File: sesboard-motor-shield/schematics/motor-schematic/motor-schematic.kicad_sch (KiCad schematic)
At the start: 0 parts

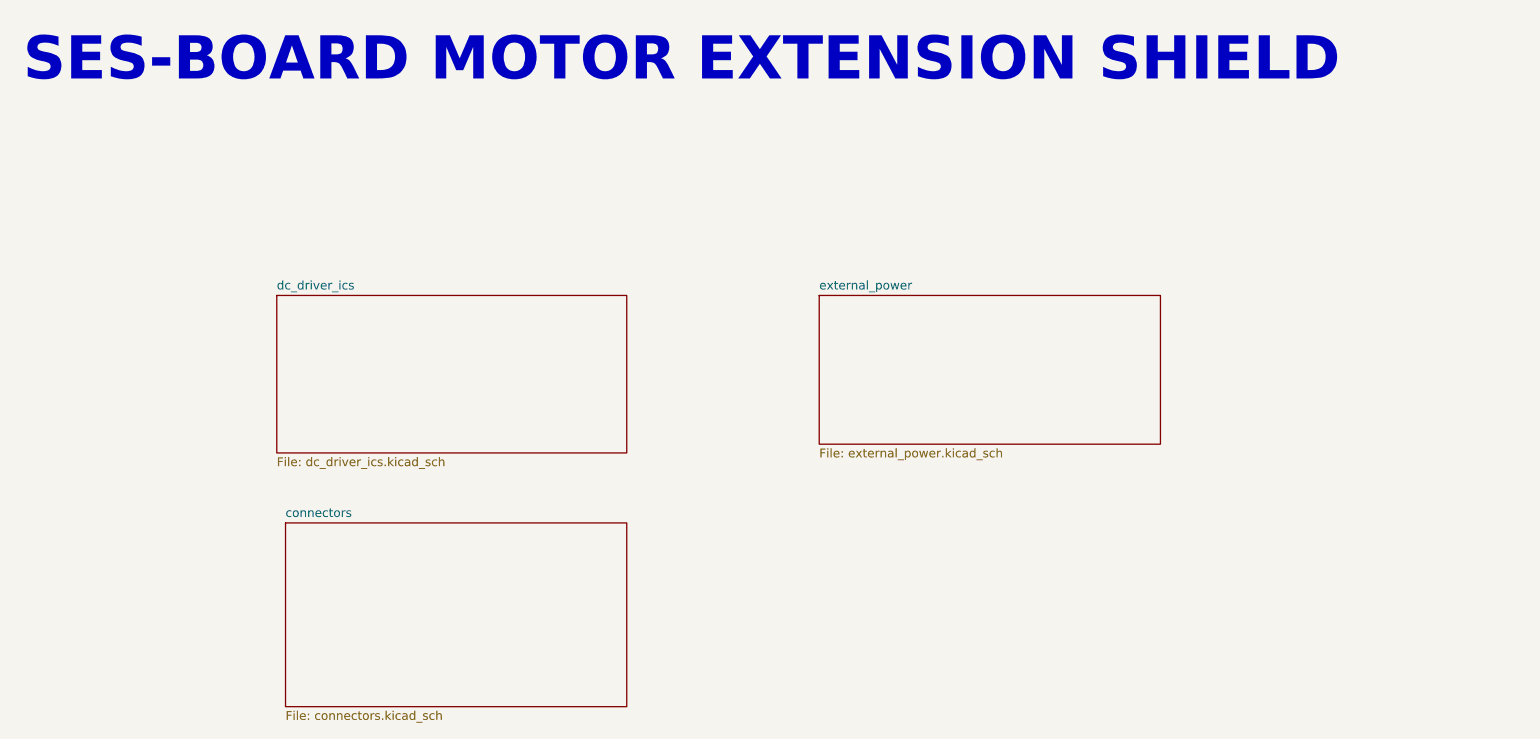
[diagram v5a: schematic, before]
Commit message: added power toggle
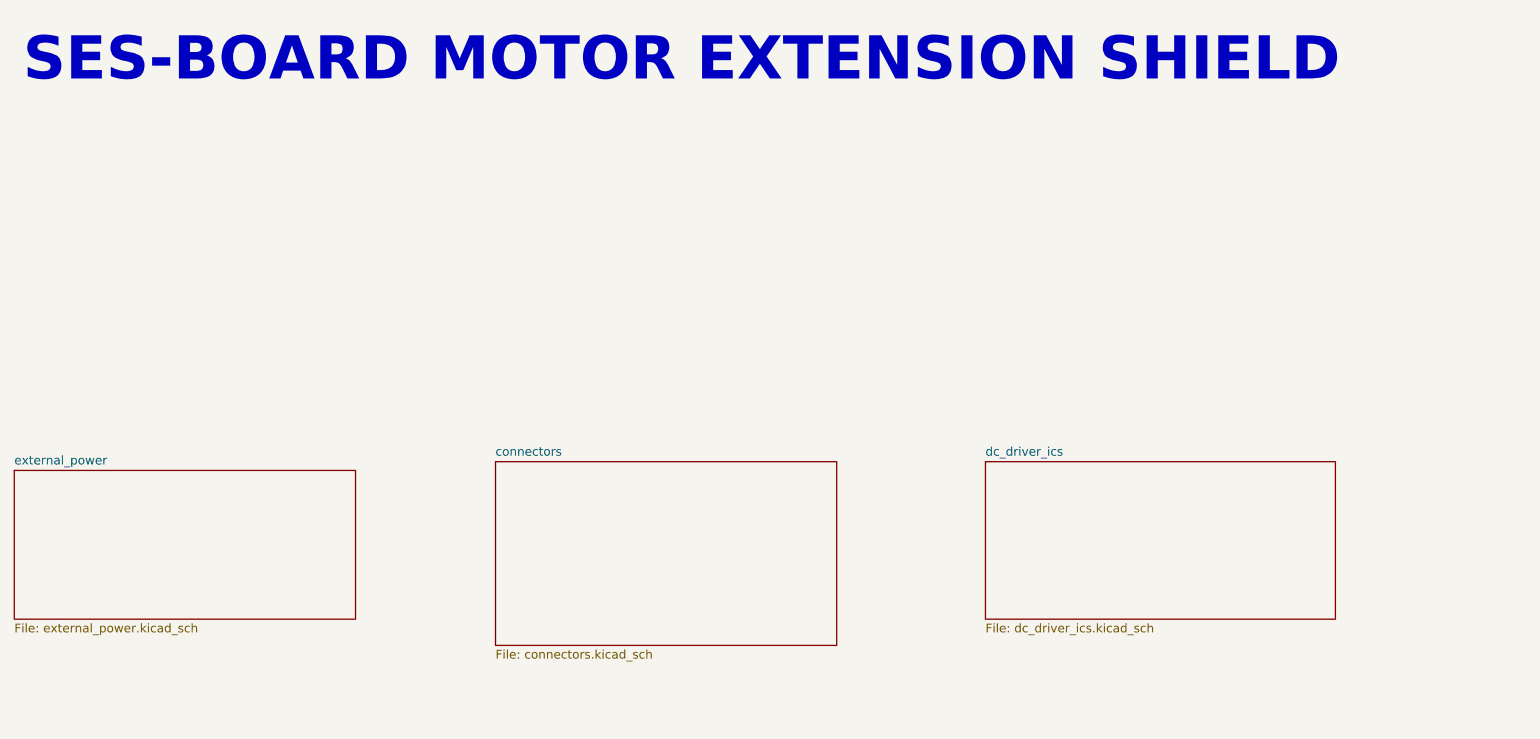
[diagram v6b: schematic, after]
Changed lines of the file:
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@@
     (effects (font (size 6.27 6.27) (thickness 1.254) bold) (justify left bottom))
   )
-  (sheet (at 90.17 102.87) (size 49.53 26.67) (fields_autoplaced)
+  (sheet (at 120.65 93.98) (size 49.53 26.67) (fields_autoplaced)
     (stroke (width 0.1524) (type solid) (color 0 0 0 0))
     (fill (color 0 0 0 0.0000))
-    (property "Sheet name" "connectors" (id 0) (at 90.17 102.1584 0)
+    (property "Sheet name" "connectors" (id 0) (at 120.65 93.2684 0)
       (effects (font (size 1.27 1.27)) (justify left bottom))
     )
-    (property "Sheet file" "connectors.kicad_sch" (id 1) (at 90.17 130.1246 0)
+    (property "Sheet file" "connectors.kicad_sch" (id 1) (at 120.65 121.2346 0)
       (effects (font (size 1.27 1.27)) (justify left top))
     )
   )
-  (sheet (at 167.64 69.85) (size 49.53 21.59) (fields_autoplaced)
+  (sheet (at 50.8 95.25) (size 49.53 21.59) (fields_autoplaced)
     (stroke (width 0.1524) (type solid) (color 0 0 0 0))
     (fill (color 0 0 0 0.0000))
-    (property "Sheet name" "external_power" (id 0) (at 167.64 69.1384 0)
+    (property "Sheet name" "external_power" (id 0) (at 50.8 94.5384 0)
       (effects (font (size 1.27 1.27)) (justify left bottom))
     )
-    (property "Sheet file" "external_power.kicad_sch" (id 1) (at 167.64 92.0246 0)
+    (property "Sheet file" "external_power.kicad_sch" (id 1) (at 50.8 117.4246 0)
       (effects (font (size 1.27 1.27)) (justify left top))
     )
   )
-  (sheet (at 88.9 69.85) (size 50.8 22.86) (fields_autoplaced)
+  (sheet (at 191.77 93.98) (size 50.8 22.86) (fields_autoplaced)
     (stroke (width 0.1524) (type solid) (color 0 0 0 0))
     (fill (color 0 0 0 0.0000))
-    (property "Sheet name" "dc_driver_ics" (id 0) (at 88.9 69.1384 0)
+    (property "Sheet name" "dc_driver_ics" (id 0) (at 191.77 93.2684 0)
       (effects (font (size 1.27 1.27)) (justify left bottom))
     )
-    (property "Sheet file" "dc_driver_ics.kicad_sch" (id 1) (at 88.9 93.2946 0)
+    (property "Sheet file" "dc_driver_ics.kicad_sch" (id 1) (at 191.77 117.4246 0)
       (effects (font (size 1.27 1.27)) (justify left top))
     )
@@
       (reference "#FLG0101") (unit 1) (value "PWR_FLAG") (footprint "")
     )
-    (path "/93d2313f-0919-4c6f-b07d-ab630442d056/44bbd26f-0500-46ae-abfb-63cd4546c073"
-      (reference "#FLG0102") (unit 1) (value "PWR_FLAG") (footprint "")
-    )
-    (path "/eeff06ce-5dd6-48ad-98cf-4489d7624b9c/d9ec88b7-2105-475b-93ae-b288bb456882"
-      (reference "#FLG0103") (unit 1) (value "PWR_FLAG") (footprint "")
+    (path "/eeff06ce-5dd6-48ad-98cf-4489d7624b9c/12da77fe-363e-47e0-af87-73a5fcdabf7c"
+      (reference "#FLG0104") (unit 1) (value "PWR_FLAG") (footprint "")
     )
     (path "/93d2313f-0919-4c6f-b07d-ab630442d056/a75ef933-e076-4304-bc85-8ec712c3ecc7"
@@
       (reference "#PWR04") (unit 1) (value "GND") (footprint "")
     )
-    (path "/93d2313f-0919-4c6f-b07d-ab630442d056/0401a85a-58aa-4a9e-bae6-f154a7963c8e"
-      (reference "#PWR05") (unit 1) (value "GND") (footprint "")
-    )
     (path "/93d2313f-0919-4c6f-b07d-ab630442d056/9e7b7e18-969a-4849-aabf-3ced45feda05"
       (reference "#PWR06") (unit 1) (value "GND") (footprint "")
@@
       (reference "#PWR010") (unit 1) (value "GND") (footprint "")
     )
-    (path "/eeff06ce-5dd6-48ad-98cf-4489d7624b9c/41dc5549-52df-4102-b74d-a5734e1fd393"
-      (reference "#PWR011") (unit 1) (value "GND") (footprint "")
-    )
     (path "/eeff06ce-5dd6-48ad-98cf-4489d7624b9c/c9b11868-444e-4002-bc99-76a2f927cee1"
       (reference "#PWR012") (unit 1) (value "GND") (footprint "")
@@
       (reference "#PWR025") (unit 1) (value "+5V") (footprint "")
     )
-    (path "/14cc8e54-6739-4c6f-a4bf-829f53e763f8/3361482c-ca19-4873-b4a9-88f85f1328a1"
-      (reference "#PWR026") (unit 1) (value "+12V") (footprint "")
-    )
     (path "/14cc8e54-6739-4c6f-a4bf-829f53e763f8/ee364f86-35f5-4a6a-be4e-6ca29ce79c84"
       (reference "#PWR0101") (unit 1) (value "GND") (footprint "")
@@
       (reference "#PWR0102") (unit 1) (value "GND") (footprint "")
     )
+    (path "/93d2313f-0919-4c6f-b07d-ab630442d056/12bc84b5-4070-44c6-8b00-b0c7cfefa04b"
+      (reference "#PWR?") (unit 1) (value "GND") (footprint "")
+    )
     (path "/93d2313f-0919-4c6f-b07d-ab630442d056/d9ead9ee-c345-4017-a86b-e222369cda3f"
-      (reference "C1") (unit 1) (value "C") (footprint "Capacitor_SMD:C_0603_1608Metric")
+      (reference "C1") (unit 1) (value "1uF") (footprint "Capacitor_SMD:C_0603_1608Metric")
     )
     (path "/93d2313f-0919-4c6f-b07d-ab630442d056/5275729a-412a-4aea-939f-ed3f5e37f264"
@@
       (reference "C5") (unit 1) (value "100nF") (footprint "Capacitor_SMD:C_0603_1608Metric_Pad1.08x0.95mm_HandSolder")
     )
+    (path "/93d2313f-0919-4c6f-b07d-ab630442d056/eb5839e2-f331-4702-9d86-67f3ade85b48"
+      (reference "C6") (unit 1) (value "0.1uF") (footprint "Capacitor_SMD:C_0603_1608Metric")
+    )
+    (path "/93d2313f-0919-4c6f-b07d-ab630442d056/6037363d-d1fc-4f28-aebc-691de39753fb"
+      (reference "C?") (unit 1) (value "10uF") (footprint "Capacitor_SMD:C_0603_1608Metric")
+    )
+    (path "/93d2313f-0919-4c6f-b07d-ab630442d056/98d131c5-bc82-4ef4-b619-001db9744aba"
+      (reference "C?") (unit 1) (value "10uF") (footprint "Capacitor_SMD:C_0603_1608Metric")
+    )
+    (path "/93d2313f-0919-4c6f-b07d-ab630442d056/dd7dcb83-d9c5-4363-9cb4-bbbb57c934ef"
+      (reference "C?") (unit 1) (value "10uF") (footprint "Capacitor_SMD:C_0603_1608Metric")
+    )
+    (path "/93d2313f-0919-4c6f-b07d-ab630442d056/e385126c-64bd-48b7-bfda-e1c7e096b966"
+      (reference "C?") (unit 1) (value "10uF") (footprint "Capacitor_SMD:C_0603_1608Metric")
+    )
     (path "/93d2313f-0919-4c6f-b07d-ab630442d056/001a0253-6ecf-4292-a1f7-0f48edbbd35b"
       (reference "D1") (unit 1) (value "GREEN_LED") (footprint "LED_SMD:LED_0603_1608Metric")
     )
-    (path "/93d2313f-0919-4c6f-b07d-ab630442d056/4f9418ba-9c6a-4f02-80b5-4d8b68173369"
-      (reference "J1") (unit 1) (value "Barrel_Jack") (footprint "Connector_BarrelJack:BarrelJack_Horizontal")
-    )
-    (path "/eeff06ce-5dd6-48ad-98cf-4489d7624b9c/c4453281-59ee-47d3-bd52-06aeb5935aac"
-      (reference "J2") (unit 1) (value "EXTERNAL_MOTOR_POWER") (footprint "TerminalBlock_Phoenix:TerminalBlock_Phoenix_MKDS-1,5-2_1x02_P5.00mm_Horizontal")
-    )
-    (path "/14cc8e54-6739-4c6f-a4bf-829f53e763f8/44d56e02-6f8b-4dba-a8f7-8cd6249ad3f6"
-      (reference "J3") (unit 1) (value "SESBOARD_LEFT") (footprint "Connector_PinHeader_2.54mm:PinHeader_1x20_P2.54mm_Vertical")
-    )
-    (path "/14cc8e54-6739-4c6f-a4bf-829f53e763f8/39b0c1e4-ee0a-4f72-8579-c96723a96d17"
-      (reference "J4") (unit 1) (value "SESBOARD_RIGHT") (footprint "Connector_PinHeader_2.54mm:PinHeader_1x20_P2.54mm_Vertical")
+    (path "/14cc8e54-6739-4c6f-a4bf-829f53e763f8/049a60b5-4d14-4cf4-af37-a2fcd4c8fbfa"
+      (reference "J3") (unit 1) (value "Conn_01x20_Female") (footprint "Connector_PinHeader_2.54mm:PinHeader_1x20_P2.54mm_Vertical")
+    )
+    (path "/14cc8e54-6739-4c6f-a4bf-829f53e763f8/9ebe7a61-acd9-4fdf-8328-f7155f17cbf2"
+      (reference "J4") (unit 1) (value "Conn_01x20_Female") (footprint "Connector_PinHeader_2.54mm:PinHeader_1x20_P2.54mm_Vertical")
     )
     (path "/14cc8e54-6739-4c6f-a4bf-829f53e763f8/82cd7066-e005-4122-a8f7-cfba4499e454"
@@
       (reference "J11") (unit 1) (value "STEPPER_TERMINAL") (footprint "Connector_PinHeader_2.54mm:PinHeader_1x05_P2.54mm_Vertical")
     )
+    (path "/93d2313f-0919-4c6f-b07d-ab630442d056/8bf5d464-b17a-4894-b669-024ae3131756"
+      (reference "J?") (unit 1) (value "PWR_TOGGLE") (footprint "")
+    )
+    (path "/93d2313f-0919-4c6f-b07d-ab630442d056/b5058be5-c3f1-4041-9886-9aa013361179"
+      (reference "J?") (unit 1) (value "EXTERNAL_MOTOR_POWER") (footprint "TerminalBlock_Phoenix:TerminalBlock_Phoenix_MKDS-1,5-2_1x02_P5.00mm_Horizontal")
+    )
     (path "/93d2313f-0919-4c6f-b07d-ab630442d056/ca07bcf5-811d-46aa-b849-0684aa3a6067"
       (reference "Q1") (unit 1) (value "Q_NMOS_DGS") (footprint "Package_TO_SOT_THT:TO-220-3_Vertical")
     )
     (path "/93d2313f-0919-4c6f-b07d-ab630442d056/a6d7f9c6-9504-4931-812e-d87c7d38a45c"
-      (reference "Q2") (unit 1) (value "TIP3055") (footprint "Package_TO_SOT_THT:TO-218-3_Vertical")
+      (reference "Q2") (unit 1) (value "TIP3055") (footprint "Package_TO_SOT_THT:TO-220-3_Vertical")
     )
     (path "/93d2313f-0919-4c6f-b07d-ab630442d056/e1d19d1a-90fd-4b02-851d-0f8a39066db3"
-      (reference "R1") (unit 1) (value "510R") (footprint "Resistor_SMD:R_0603_1608Metric")
+      (reference "R1") (unit 1) (value "240R") (footprint "Resistor_SMD:R_0603_1608Metric")
     )
     (path "/93d2313f-0919-4c6f-b07d-ab630442d056/06f09c2f-89c0-45c5-9ecb-66d7577cc34e"
-      (reference "R2") (unit 1) (value "510R") (footprint "Resistor_SMD:R_0603_1608Metric")
-    )
-    (path "/93d2313f-0919-4c6f-b07d-ab630442d056/e1320052-63b8-4d04-a3b1-99858ebf302c"
-      (reference "RV1") (unit 1) (value "R_Potentiometer_Trim_US") (footprint "Potentiometer_SMD:Potentiometer_Vishay_TS53YL_Vertical")
+      (reference "R2") (unit 1) (value "2K") (footprint "Resistor_SMD:R_0603_1608Metric")
+    )
+    (path "/93d2313f-0919-4c6f-b07d-ab630442d056/14e13612-5917-4953-8011-6fde0a6a2bba"
+      (reference "R3") (unit 1) (value "2K") (footprint "Resistor_SMD:R_0603_1608Metric")
     )
     (path "/93d2313f-0919-4c6f-b07d-ab630442d056/ae0756d7-ed93-4874-bb3b-1e5d145ea0a5"
@@
       (reference "U5") (unit 1) (value "L293D") (footprint "Package_DIP:DIP-16_W7.62mm")
     )
-  )
+    (path "/93d2313f-0919-4c6f-b07d-ab630442d056/f75b0e9c-6b98-4328-b297-b8b9e2738282"
+      (reference "U?") (unit 1) (value "AMS1117-3.3") (footprint "Package_TO_SOT_SMD:SOT-223-3_TabPin2")
+    )
+  )
